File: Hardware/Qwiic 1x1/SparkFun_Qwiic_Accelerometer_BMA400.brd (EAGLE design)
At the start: 25.4 x 25.4 mm, 56 parts, among them J1 QWIIC_RIGHT_ANGLE, J2 QWIIC_RIGHT_ANGLE, U1 BMA400

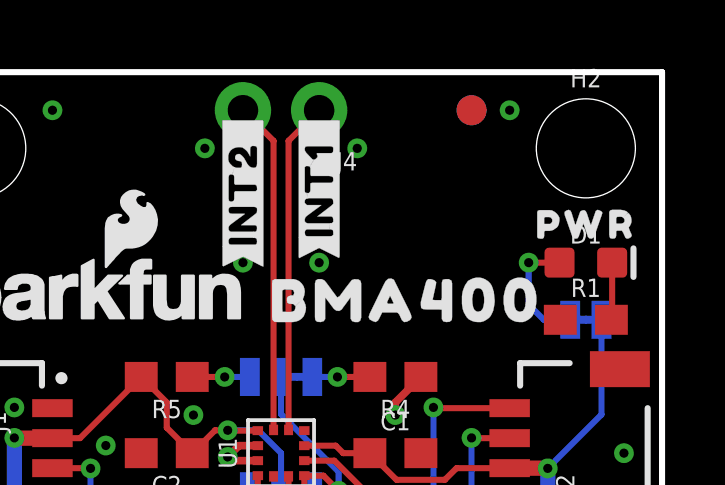
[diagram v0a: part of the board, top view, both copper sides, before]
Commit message: Add axes labels
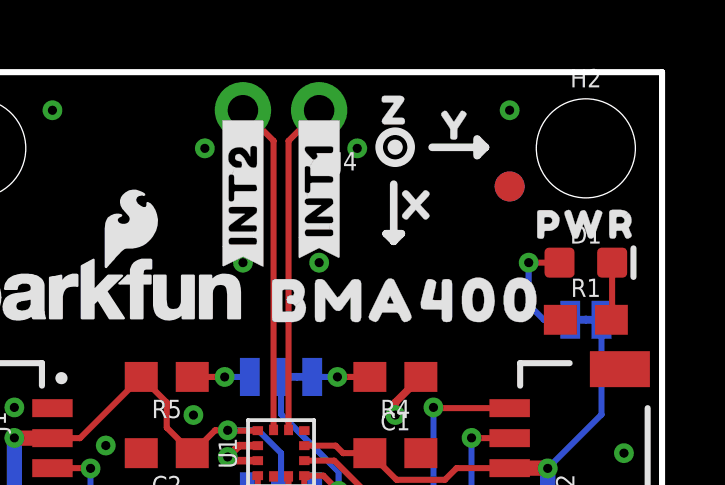
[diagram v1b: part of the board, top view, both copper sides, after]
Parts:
- added U$2, U$34: (no value), ISMTopMini:X2114
- added U$29, U$36: (no value), ISMTopMini:Z2116
- added U$3, U$35: (no value), ISMTopMini:Y2115
- moved FD1 2.84 mm to (20.3, 21.6)
- moved FD2 2.84 mm to (20.3, 21.6)
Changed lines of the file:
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@@
 <dimension x1="0" y1="25.4" x2="13.97" y2="25.4" x3="6.985" y3="30.48" textsize="1.778" layer="47" unit="inch"/>
 <text x="-17.78" y="-2.54" size="1.778" layer="47" font="vector">Units: inches</text>
+<wire x1="16.456025" y1="19.7612" x2="16.456025" y2="21.6662" width="0.254" layer="21"/>
+<wire x1="16.456025" y1="19.7612" x2="16.710025" y2="20.0152" width="0.254" layer="21"/>
+<wire x1="16.456025" y1="19.7612" x2="16.202025" y2="20.0152" width="0.254" layer="21"/>
+<wire x1="19.51355" y1="22.894925" x2="17.73555" y2="22.894925" width="0.254" layer="21"/>
+<wire x1="19.51355" y1="22.894925" x2="19.25955" y2="23.148925" width="0.254" layer="21"/>
+<wire x1="19.51355" y1="22.894925" x2="19.25955" y2="22.640925" width="0.254" layer="21"/>
+<wire x1="19.23415" y1="23.174325" x2="19.23415" y2="22.615525" width="0.254" layer="21"/>
+<wire x1="16.202025" y1="20.0152" x2="16.710025" y2="20.0152" width="0.254" layer="21"/>
+<circle x="16.50365" y="22.8981" radius="0.127" width="0.254" layer="21"/>
+<circle x="16.50365" y="22.8981" radius="0.5334" width="0.254" layer="21"/>
+<wire x1="16.436975" y1="19.7612" x2="16.436975" y2="21.6662" width="0.254" layer="22"/>
+<wire x1="16.436975" y1="19.7612" x2="16.182975" y2="20.0152" width="0.254" layer="22"/>
+<wire x1="16.436975" y1="19.7612" x2="16.690975" y2="20.0152" width="0.254" layer="22"/>
+<wire x1="19.51355" y1="22.825075" x2="17.73555" y2="22.825075" width="0.254" layer="22"/>
+<wire x1="19.51355" y1="22.825075" x2="19.25955" y2="22.571075" width="0.254" layer="22"/>
+<wire x1="19.51355" y1="22.825075" x2="19.25955" y2="23.079075" width="0.254" layer="22"/>
+<wire x1="19.23415" y1="22.545675" x2="19.23415" y2="23.104475" width="0.254" layer="22"/>
+<wire x1="16.690975" y1="20.0152" x2="16.182975" y2="20.0152" width="0.254" layer="22"/>
+<circle x="16.51635" y="22.8981" radius="0.5334" width="0.254" layer="22"/>
+<wire x1="16.1464625" y1="22.5663125" x2="16.8608375" y2="23.2806875" width="0.2032" layer="22"/>
+<wire x1="16.1464625" y1="23.241" x2="16.8608375" y2="22.526625" width="0.2032" layer="22"/>
 </plain>
 <attributes>
@@
 <element name="LOGO2" library="SparkFun-Aesthetics" package="SFE_LOGO_NAME_FLAME_.1" value="SFE_LOGO_NAME_FLAME.1_INCH" x="5.969" y="17.78" smashed="yes"/>
 <element name="LOGO3" library="SparkFun-Aesthetics" package="OSHW-LOGO-S" value="OSHW-LOGOS" x="22.86" y="7.62" smashed="yes"/>
-<element name="FD1" library="SparkFun-Aesthetics" package="FIDUCIAL-1X2" value="FIDUCIAL1X2" x="19.05" y="24.13" smashed="yes"/>
-<element name="FD2" library="SparkFun-Aesthetics" package="FIDUCIAL-1X2" value="FIDUCIAL1X2" x="19.05" y="24.13" smashed="yes" rot="MR0"/>
+<element name="FD1" library="SparkFun-Aesthetics" package="FIDUCIAL-1X2" value="FIDUCIAL1X2" x="20.32" y="21.59" smashed="yes"/>
+<element name="FD2" library="SparkFun-Aesthetics" package="FIDUCIAL-1X2" value="FIDUCIAL1X2" x="20.32" y="21.59" smashed="yes" rot="MR0"/>
 <element name="FD3" library="SparkFun-Aesthetics" package="FIDUCIAL-1X2" value="FIDUCIAL1X2" x="1.27" y="6.35" smashed="yes" rot="MR0"/>
 <element name="FD4" library="SparkFun-Aesthetics" package="FIDUCIAL-1X2" value="FIDUCIAL1X2" x="1.27" y="6.35" smashed="yes"/>
@@
 <attribute name="VALUE" x="12.7" y="16.383" size="0.6096" layer="28" font="vector" ratio="20" rot="MR180" align="top-center"/>
 </element>
+<element name="U$34" library="ISMTopMini" package="X2114" value="" x="17.272" y="20.955" smashed="yes"/>
+<element name="U$35" library="ISMTopMini" package="Y2115" value="" x="18.542" y="23.622" smashed="yes"/>
+<element name="U$36" library="ISMTopMini" package="Z2116" value="" x="16.51" y="24.13" smashed="yes"/>
+<element name="U$2" library="ISMTopMini" package="X2114" value="" x="17.145" y="20.955" smashed="yes" rot="MR0"/>
+<element name="U$3" library="ISMTopMini" package="Y2115" value="" x="18.415" y="23.622" smashed="yes" rot="MR0"/>
+<element name="U$29" library="ISMTopMini" package="Z2116" value="" x="16.51" y="24.13" smashed="yes" rot="MR0"/>
 </elements>
 <signals>

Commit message: Update version number to v10
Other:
- board text added: "v10"
- board text removed: "v01"
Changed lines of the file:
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@@
 <wire x1="0" y1="25.4" x2="0" y2="0" width="0.2032" layer="20"/>
 <rectangle x1="11.8618" y1="12.6746" x2="11.9888" y2="12.7508" layer="41"/>
-<text x="1.27" y="10.16" size="1.778" layer="16" font="vector" ratio="15" rot="MR270" align="center">v01</text>
+<text x="1.27" y="10.16" size="1.778" layer="16" font="vector" ratio="15" rot="MR270" align="center">v10</text>
 <rectangle x1="11.43" y1="13.716" x2="11.684" y2="14.351" layer="42"/>
 <text x="16.51" y="-29.21" size="1.778" layer="51" font="vector">Dryw Wade</text>

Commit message: Remove library file
Part is in SFE Eagle library, update part in design
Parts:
- U1: device BMA400:BMA400 -> SparkFun-Sensors:BMA400
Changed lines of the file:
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@@
 <attribute name="REV" value="" x="69.85" y="-30.48" size="1.778" layer="27" display="off"/>
 </element>
-<element name="U1" library="BMA400" package="BMA400" value="BMA400" x="12.7" y="12.7" smashed="yes" rot="R90">
+<element name="U1" library="SparkFun-Sensors" package="BMA400" value="BMA400" x="12.7" y="12.7" smashed="yes" rot="R90">
 <attribute name="NAME" x="10.922" y="12.7" size="0.6096" layer="25" font="vector" ratio="20" rot="R90" align="center"/>
 <attribute name="PROD_ID" value="IC-17118" x="12.7" y="12.7" size="1.778" layer="27" rot="R90" display="off"/>
